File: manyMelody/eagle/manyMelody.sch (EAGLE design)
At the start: 13 parts, among them IC1 788TV

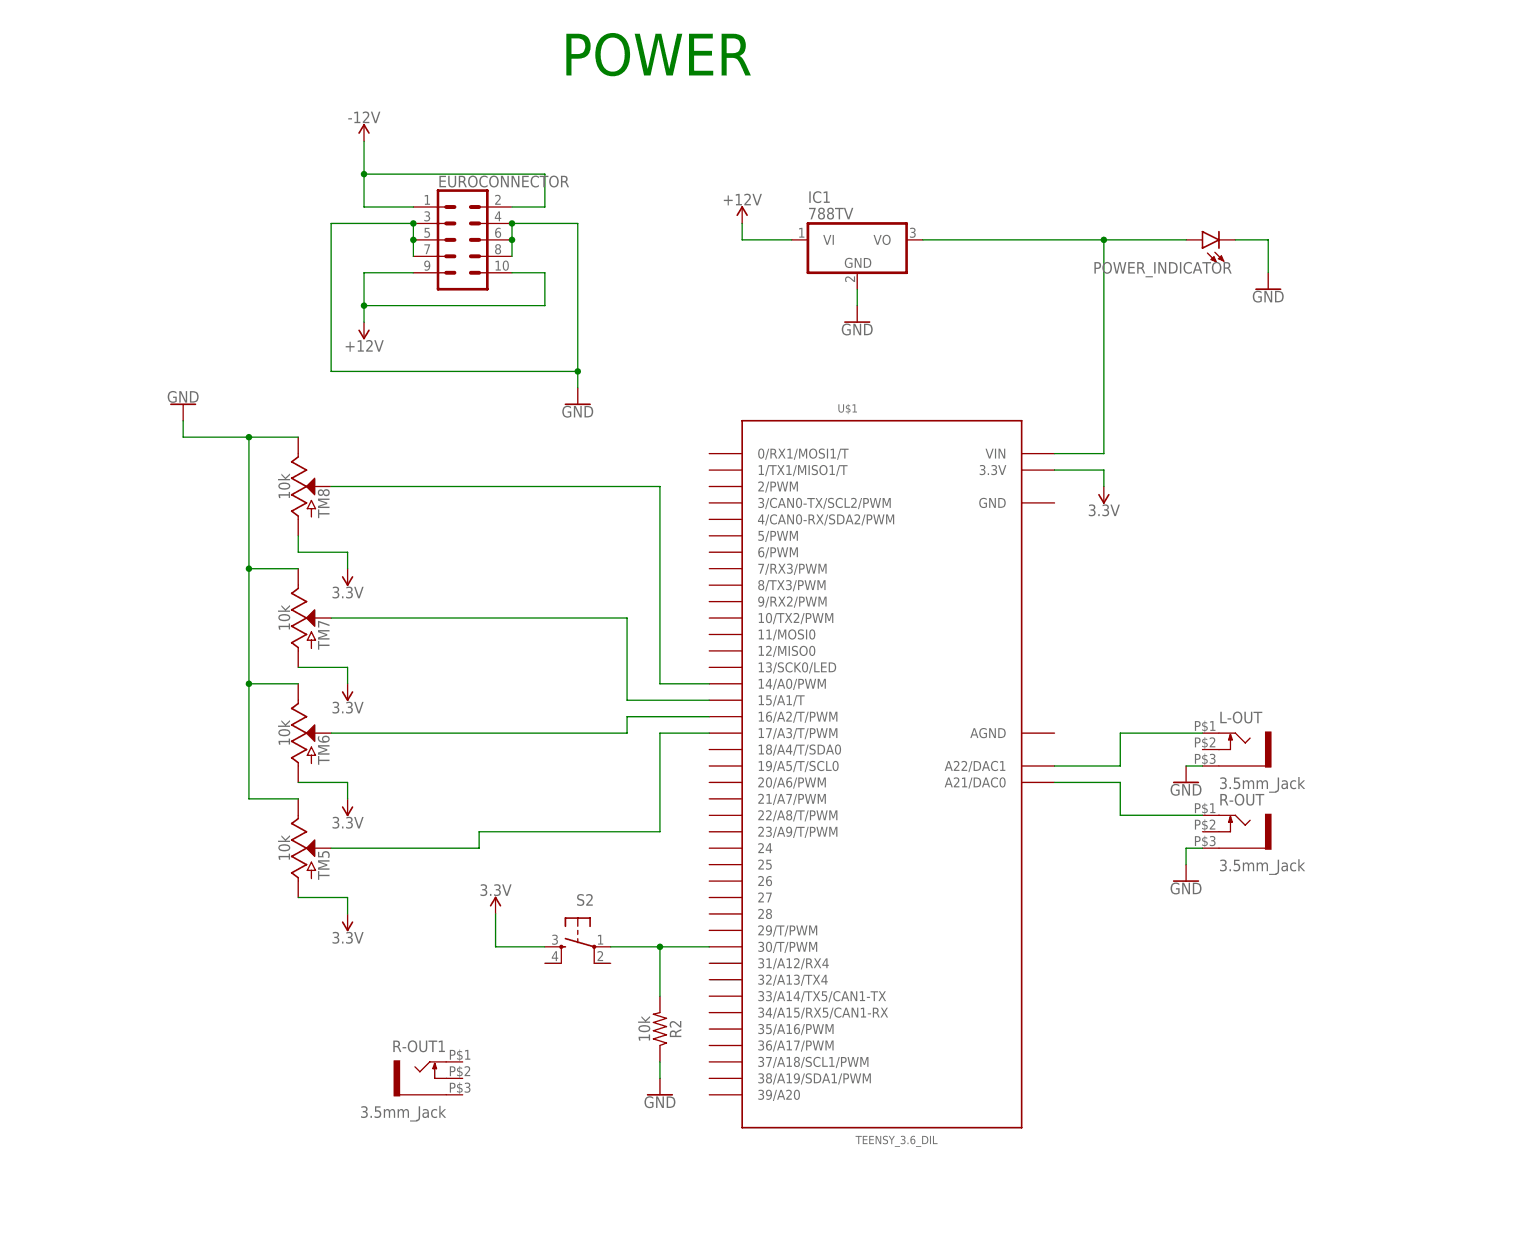
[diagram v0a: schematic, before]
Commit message: adjusted input pin definitions for teensy and for stereo output
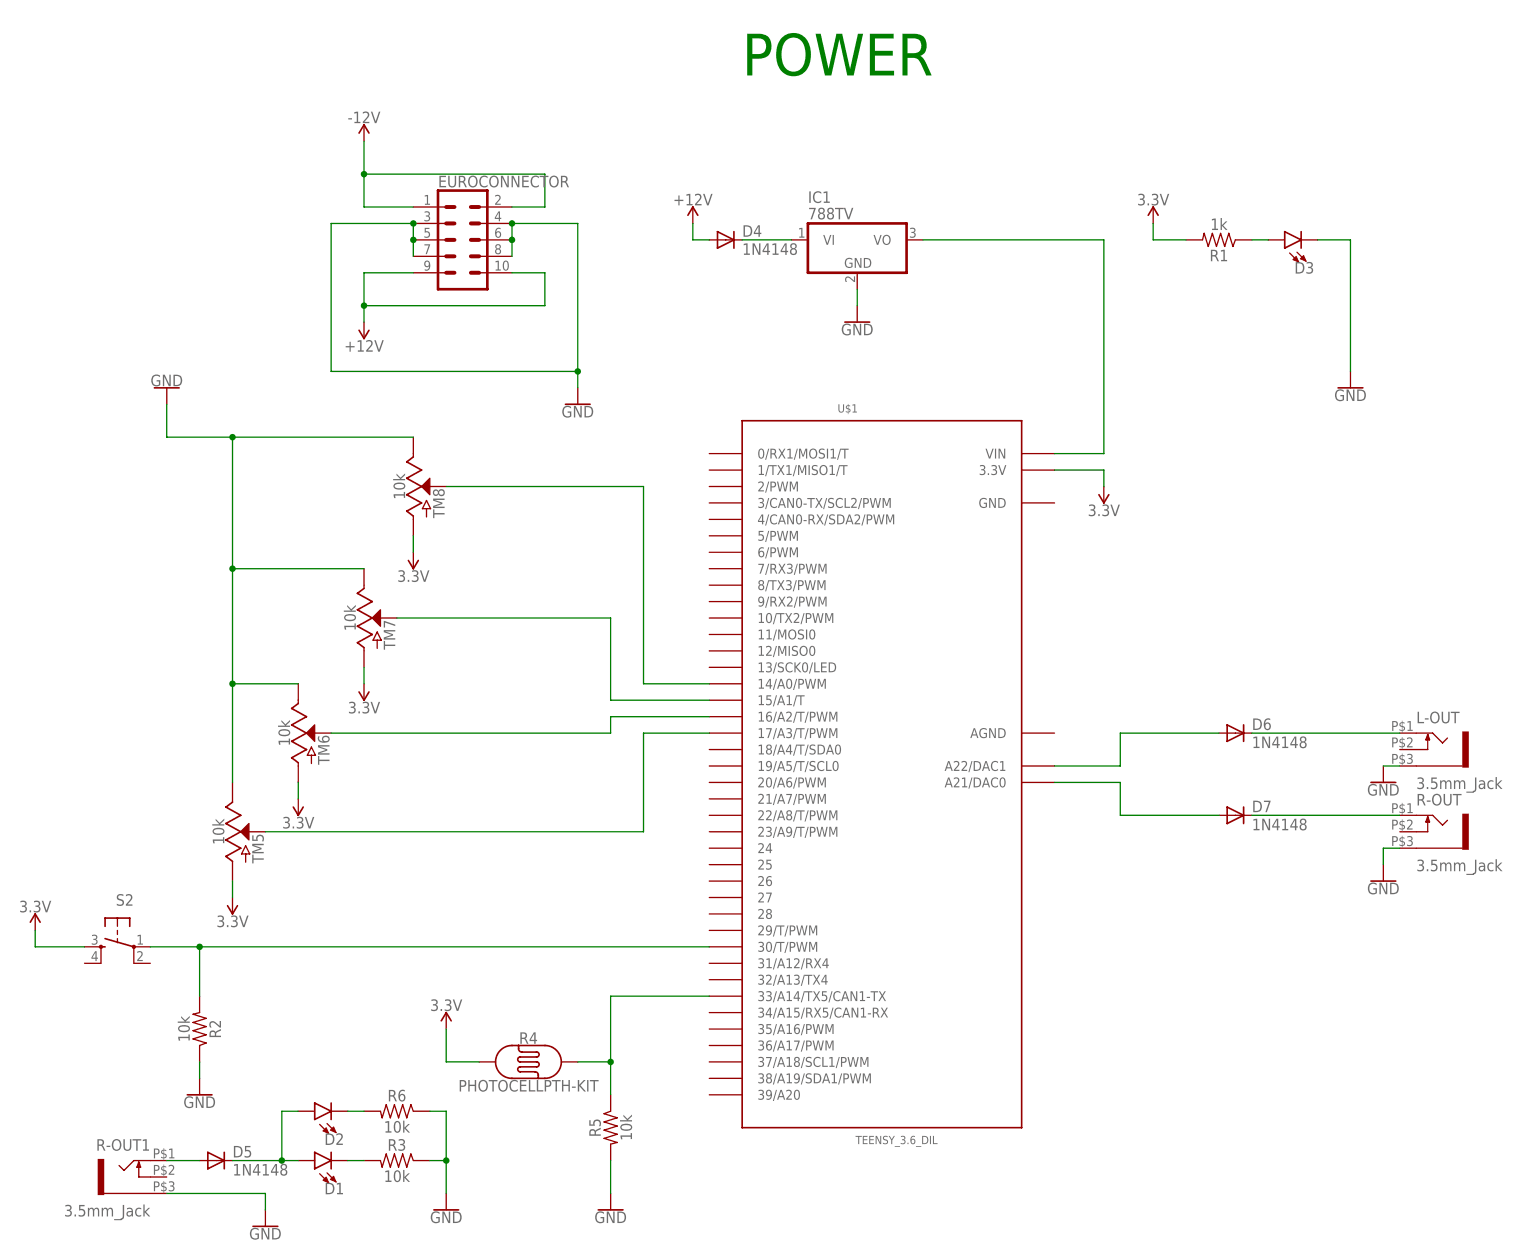
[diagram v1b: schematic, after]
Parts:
- removed POWER_INDICATOR: (no value), SparkFun-LED:LED5MM
- added D1, D2, D3: (no value), SparkFun-LED:LED-3MM-NO_SILK
- added D4, D5, D6, D7: 1N4148, diode:1N4004
- added R1: 1k, SparkFun-Resistors:1KOHM-HORIZ-1/4W-5%
- added R3, R5, R6: 10k, SparkFun-Resistors:1KOHM-HORIZ-1/4W-5%
- added R4: PHOTOCELLPTH-KIT, SparkFun-Sensors:PHOTOCELLPTH-KIT
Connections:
- new net N$1: D1.A, D2.A, D5.C
- new net N$15: D4.C, IC1.VI
- new net N$16: D5.A, R-OUT1.2
- new net N$2: D1.C, R3.2
- new net N$4: R4.P$2, R5.1, U$1.33/A14/TX5/CAN1-TX
- new net N$5: D2.C, R6.2
- new net N$6: D3.A, R1.1
- new net N$7: D6.C, L-OUT.2
- new net N$8: D7.C, R-OUT.2
- net +12V: now also D4.A; no longer IC1.VI
- net 3.3V: now also R1.2, R4.P$1
- net 5V: no longer POWER_INDICATOR.A
- net GND: now also D3.C, R-OUT1.1, R3.1, R5.2, R6.1; no longer POWER_INDICATOR.C
- net N$10: now also D7.A; no longer R-OUT.2
- net N$9: now also D6.A; no longer L-OUT.2
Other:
- moved on the sheet: L-OUT, R-OUT, R-OUT1, R2, S2, TM5, TM7, TM8
